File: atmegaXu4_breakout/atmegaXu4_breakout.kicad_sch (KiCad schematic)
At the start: 31 parts, among them J1 USB_C_Receptacle_USB2.0, J2 Header-West, J3 Header-East, J4 AVR-ISP-6, U1 ATmega32U4-MU, U2 AP2127K-3.3, Y1 ABM11-16.000MHZ-12-N1G-T

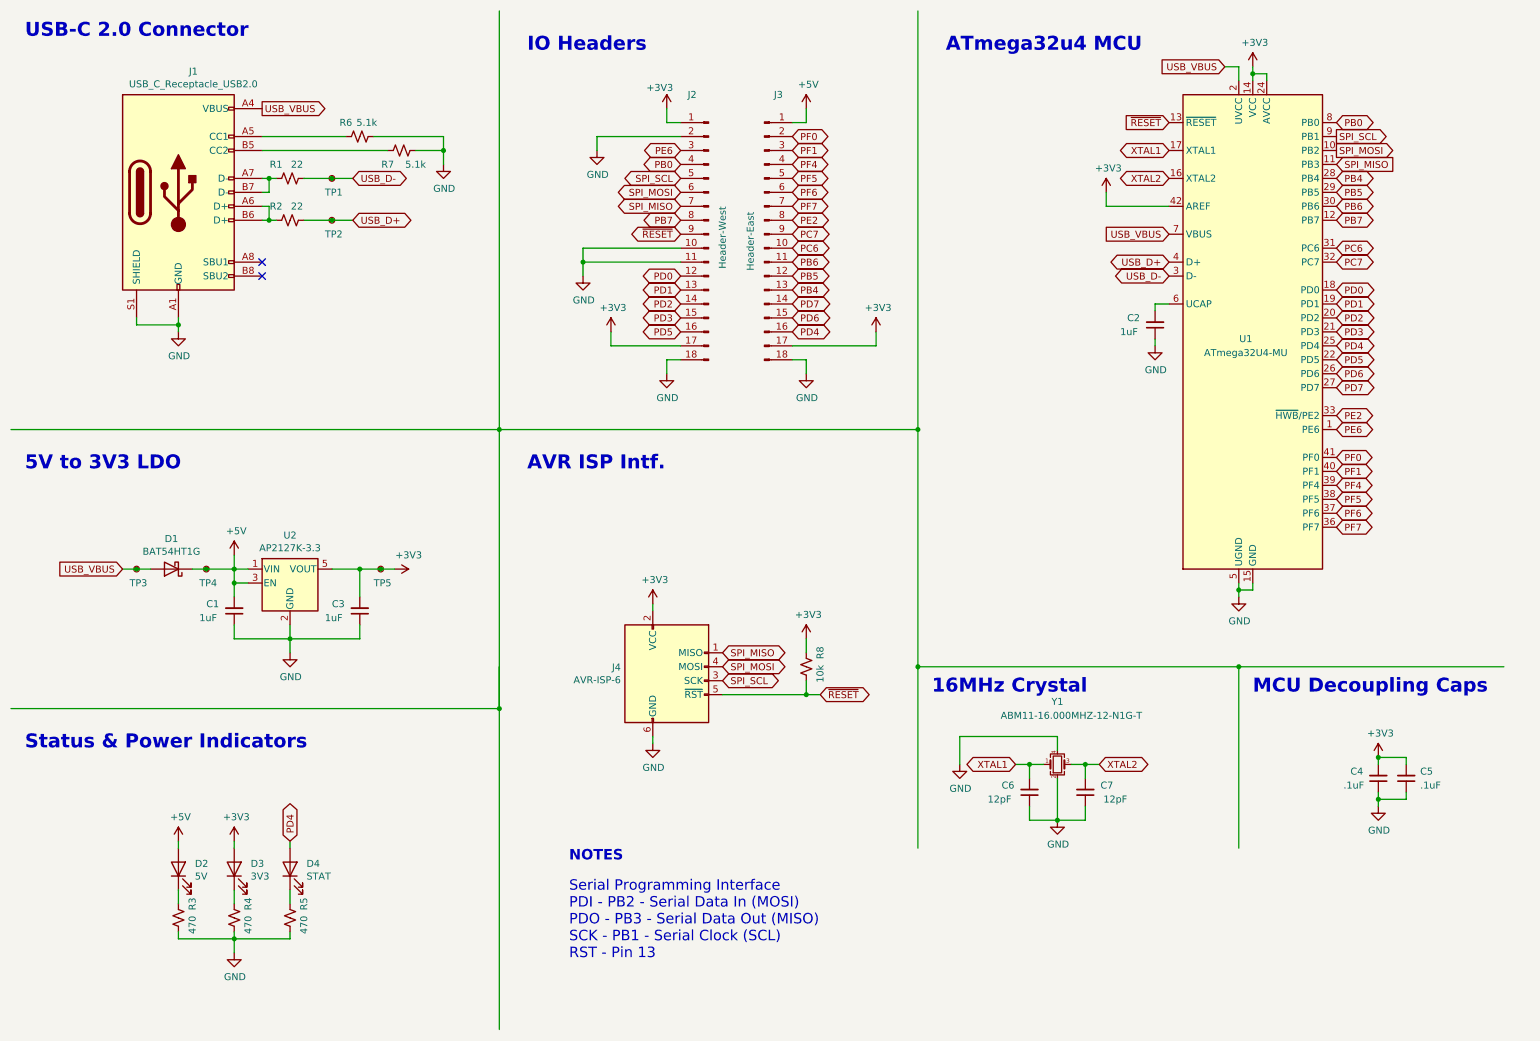
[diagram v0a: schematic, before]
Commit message: Added nRST and nUSR push-buttons
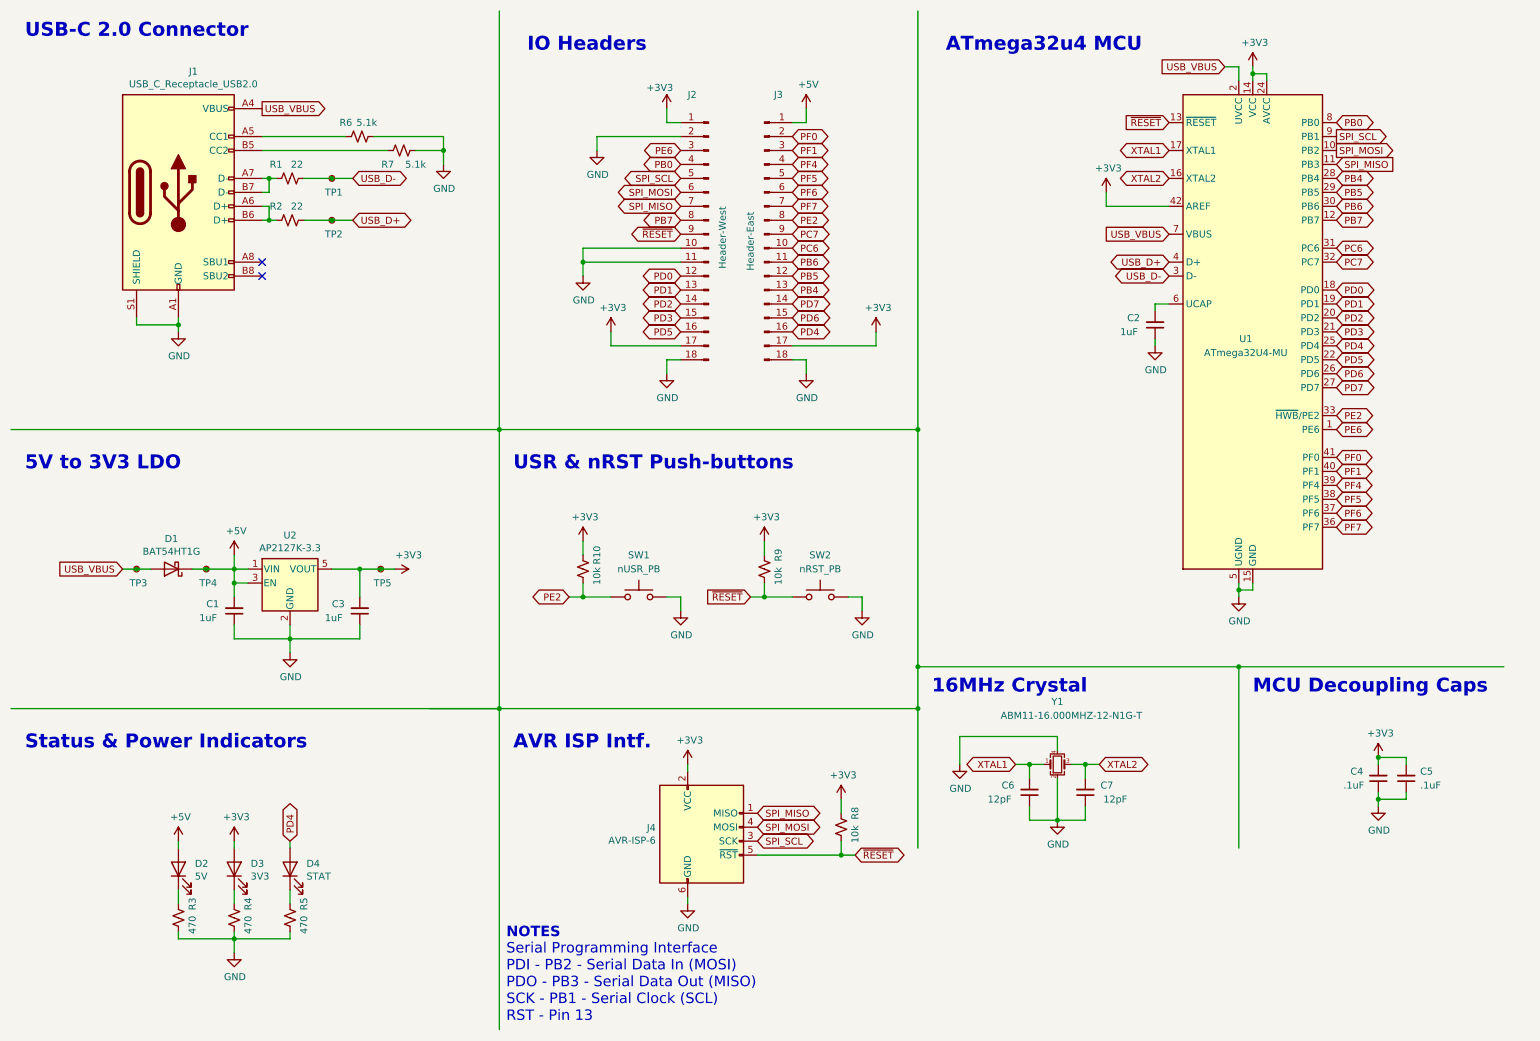
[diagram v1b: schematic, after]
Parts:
- added R10, R9: 10k, Resistor_SMD:R_0402_1005Metric, symbol Device:R_Small_US
- added SW1: nUSR_PB, Button_Switch_SMD:SW_Push_1P1T_NO_CK_KMR2, symbol Switch:SW_Push
- added SW2: nRST_PB, Button_Switch_SMD:SW_Push_1P1T_NO_CK_KMR2, symbol Switch:SW_Push
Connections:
- net +3V3: now also R10.2, R9.2
- net GND: now also SW1.2, SW2.2
- net PE2: now also R10.1, SW1.1
- net ~{RESET}: now also R9.1, SW2.1
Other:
- note added: "USR & nRST Push-buttons"
- moved on the sheet: J4, R8

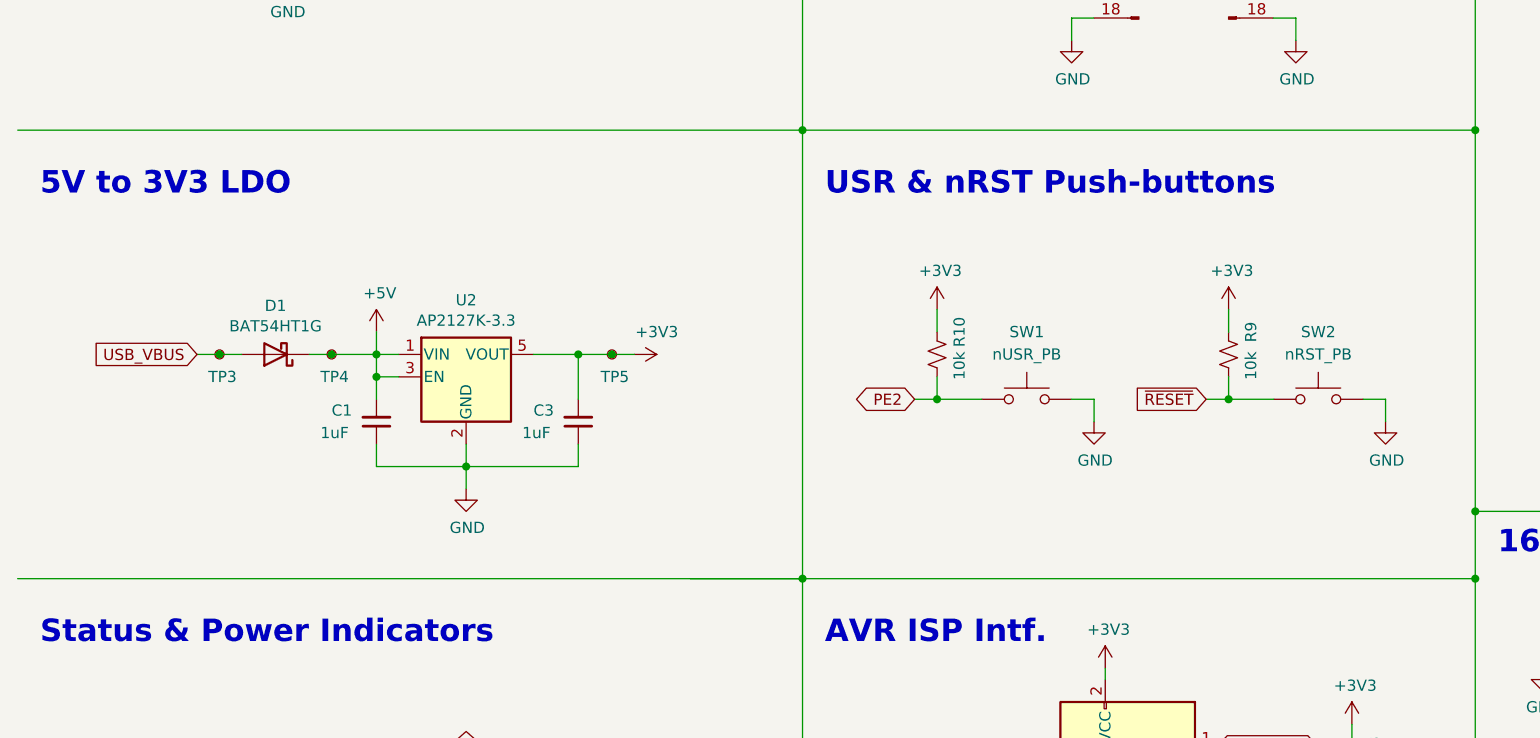
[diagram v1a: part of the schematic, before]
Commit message: Started adding MFP values for components
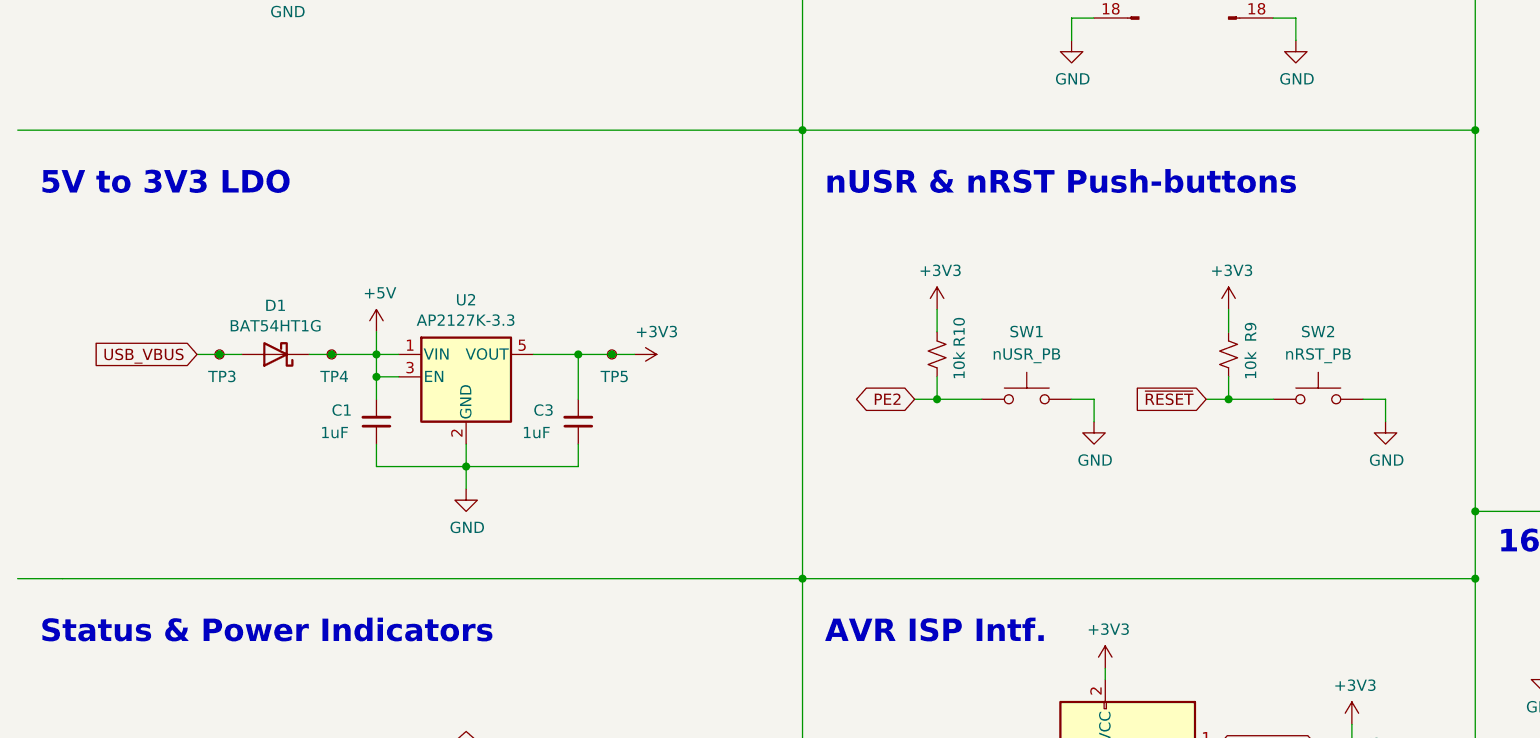
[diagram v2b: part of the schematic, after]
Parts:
- D1: MFP (none) -> BAT54HT1G
- J1: MFP (none) -> USB4085
- SW1, SW2: MFP (none) -> KMR2
- U1: MFP (none) -> ATmega32U4-MU
- U2: MFP (none) -> AP2127K-3.3
- Y1: MFP (none) -> ABM11-16.000MHZ-12-N1G-T
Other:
- note added: "nUSR & nRST Push-buttons"
- note removed: "USR & nRST Push-buttons"
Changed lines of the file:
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@@
-    (stroke (width 0) (type default))
-  )
-  (wire (pts (xy 88.9 139.7) (xy 101.6 139.7))
     (stroke (width 0) (type default))
   )
@@
     (stroke (width 0) (type default))
   )
-  (wire (pts (xy 12.7 139.7) (xy 101.6 139.7))
+  (wire (pts (xy 17.78 139.7) (xy 101.6 139.7))
     (stroke (width 0.254) (type dash))
   )
@@
     (stroke (width 0) (type default))
   )
+  (wire (pts (xy 12.7 139.7) (xy 17.78 139.7))
+    (stroke (width 0.254) (type dash))
+  )
   (wire (pts (xy 147.32 119.38) (xy 149.86 119.38))
     (stroke (width 0) (type default))
@@
     (stroke (width 0.254) (type dash))
   )
-  (text "USR & nRST Push-buttons" (at 104.14 96.52 0)
+  (text "nUSR & nRST Push-buttons" (at 104.14 96.52 0)
     (effects (font (size 2.54 2.54) (thickness 0.508) bold) (justify left bottom))
   )
@@
     )
     (property "Datasheet" "http://ww1.microchip.com/downloads/en/DeviceDoc/Atmel-7766-8-bit-AVR-ATmega16U4-32U4_Datasheet.pdf" (at 238.76 71.12 0)
+      (effects (font (size 1.27 1.27)) hide)
+    )
+    (property "MFP" "ATmega32U4-MU" (at 238.76 71.12 0)
       (effects (font (size 1.27 1.27)) hide)
     )
@@
       (effects (font (size 1.27 1.27)) hide)
     )
+    (property "MFP" "USB4085" (at 43.18 45.72 0)
+      (effects (font (size 1.27 1.27)) hide)
+    )
     (pin "A1")
     (pin "A12")
@@
       (effects (font (size 1.27 1.27)) hide)
     )
+    (property "MFP" "AP2127K-3.3" (at 63.5 116.84 0)
+      (effects (font (size 1.27 1.27)) hide)
+    )
     (pin "1")
     (pin "2")
@@
     )
     (property "Datasheet" "~" (at 41.91 114.3 0)
+      (effects (font (size 1.27 1.27)) hide)
+    )
+    (property "MFP" "BAT54HT1G" (at 41.91 114.3 0)
       (effects (font (size 1.27 1.27)) hide)
     )
@@
       (effects (font (size 1.27 1.27)) hide)
     )
+    (property "MFP" "KMR2" (at 160.02 119.38 0)
+      (effects (font (size 1.27 1.27)) hide)
+    )
     (pin "1")
     (pin "2")
@@
     )
     (property "Datasheet" "~" (at 203.2 149.86 0)
+      (effects (font (size 1.27 1.27)) hide)
+    )
+    (property "MFP" "ABM11-16.000MHZ-12-N1G-T" (at 203.2 149.86 0)
       (effects (font (size 1.27 1.27)) hide)
     )
@@
       (effects (font (size 1.27 1.27)) hide)
     )
+    (property "MFP" "KMR2" (at 127 119.38 0)
+      (effects (font (size 1.27 1.27)) hide)
+    )

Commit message: Clean DRC.
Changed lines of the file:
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@@
-(kicad_sch (version 20221206) (generator eeschema)
+(kicad_sch (version 20230121) (generator eeschema)
   (paper "A4")
   (title_block
@@
     (stroke (width 0) (type default))
   )
-  (wire (pts (xy 170.18 71.12) (xy 170.18 73.66))
+  (wire (pts (xy 165.1 71.12) (xy 165.1 73.66))
     (stroke (width 0) (type default))
   )
@@
     (stroke (width 0) (type default))
   )
-  (wire (pts (xy 154.94 73.66) (xy 170.18 73.66))
+  (wire (pts (xy 154.94 73.66) (xy 165.1 73.66))
     (stroke (width 0) (type default))
   )
@@
     (stroke (width 0) (type default))
   )
-  (wire (pts (xy 17.78 139.7) (xy 101.6 139.7))
+  (wire (pts (xy 12.7 139.7) (xy 101.6 139.7))
     (stroke (width 0.254) (type dash))
   )
@@
     (stroke (width 0) (type default))
   )
-  (wire (pts (xy 121.92 71.12) (xy 121.92 73.66))
+  (wire (pts (xy 124.46 71.12) (xy 124.46 73.66))
     (stroke (width 0) (type default))
   )
@@
     (stroke (width 0) (type default))
   )
-  (wire (pts (xy 121.92 73.66) (xy 134.62 73.66))
+  (wire (pts (xy 124.46 73.66) (xy 134.62 73.66))
     (stroke (width 0) (type default))
   )
@@
   (wire (pts (xy 59.69 45.72) (xy 59.69 43.18))
     (stroke (width 0) (type default))
-  )
-  (wire (pts (xy 12.7 139.7) (xy 17.78 139.7))
-    (stroke (width 0.254) (type dash))
   )
   (wire (pts (xy 147.32 119.38) (xy 149.86 119.38))
@@
     )
   )
-  (symbol (lib_id "power:+3V3") (at 170.18 71.12 0) (unit 1)
-    (in_bom yes) (on_board yes) (dnp no)
-    (property "Reference" "#PWR0109" (at 170.18 74.93 0)
-      (effects (font (size 1.27 1.27)) hide)
-    )
-    (property "Value" "+3V3" (at 170.561 66.7258 0)
-      (effects (font (size 1.27 1.27)))
-    )
-    (property "Footprint" "" (at 170.18 71.12 0)
-      (effects (font (size 1.27 1.27)) hide)
-    )
-    (property "Datasheet" "" (at 170.18 71.12 0)
+  (symbol (lib_id "power:+3V3") (at 165.1 71.12 0) (unit 1)
+    (in_bom yes) (on_board yes) (dnp no)
+    (property "Reference" "#PWR0109" (at 165.1 74.93 0)
+      (effects (font (size 1.27 1.27)) hide)
+    )
+    (property "Value" "+3V3" (at 165.481 66.7258 0)
+      (effects (font (size 1.27 1.27)))
+    )
+    (property "Footprint" "" (at 165.1 71.12 0)
+      (effects (font (size 1.27 1.27)) hide)
+    )
+    (property "Datasheet" "" (at 165.1 71.12 0)
       (effects (font (size 1.27 1.27)) hide)
     )
@@
     )
   )
-  (symbol (lib_id "power:+3V3") (at 121.92 71.12 0) (unit 1)
-    (in_bom yes) (on_board yes) (dnp no)
-    (property "Reference" "#PWR0111" (at 121.92 74.93 0)
-      (effects (font (size 1.27 1.27)) hide)
-    )
-    (property "Value" "+3V3" (at 122.301 66.7258 0)
-      (effects (font (size 1.27 1.27)))
-    )
-    (property "Footprint" "" (at 121.92 71.12 0)
-      (effects (font (size 1.27 1.27)) hide)
-    )
-    (property "Datasheet" "" (at 121.92 71.12 0)
-      (effects (font (size 1.27 1.27)) hide)
-    )
+  (symbol (lib_id "power:+3V3") (at 124.46 71.12 0) (unit 1)
+    (in_bom yes) (on_board yes) (dnp no)
+    (property "Reference" "#PWR0111" (at 124.46 74.93 0)
+      (effects (font (size 1.27 1.27)) hide)
+    )
+    (property "Value" "+3V3" (at 124.841 66.7258 0)
+      (effects (font (size 1.27 1.27)))
+    )
+    (property "Footprint" "" (at 124.46 71.12 0)
+      (effects (font (size 1.27 1.27)) hide)
+    )
+    (property "Datasheet" "" (at 124.46 71.12 0)
+      (effects (font (size 1.27 1.27)) hide)
+    )

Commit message: Updated silk logo to everydaydev
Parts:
- J1: MFP USB4085 -> (none); MPN (none) -> USB4085; Manufacturer (none) -> GCT
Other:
- company: great lakes dev -> everyday dev
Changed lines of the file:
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@@
   (title_block
     (title "atmega32u4_breakout")
-    (date "2022-12-27")
+    (date "2023-06-26")
     (rev "rev B")
-    (company "great lakes dev")
+    (company "everyday dev")
+    (comment 1 "os.everydaydev.io")
   )
   (junction (at 177.8 139.7) (diameter 0) (color 0 0 0 0)
@@
       (effects (font (size 1.27 1.27)) hide)
     )
-    (property "MFP" "USB4085" (at 43.18 45.72 0)
-      (effects (font (size 1.27 1.27)) hide)
-    )
+    (property "MPN" "USB4085" (at 43.18 45.72 0)
+      (effects (font (size 1.27 1.27)) hide)
+    )
+    (property "Manufacturer" "GCT" (at 43.18 45.72 0)
+      (effects (font (size 1.27 1.27)) hide)
+    )
